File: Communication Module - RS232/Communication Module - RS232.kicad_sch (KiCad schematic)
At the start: 25 parts, among them J1 PinHeader_1x02_P2.54mm_Vertic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, P31 DB25_Receptacle_MountingHoles, U1 SP232EEN, U31 SP232EEN

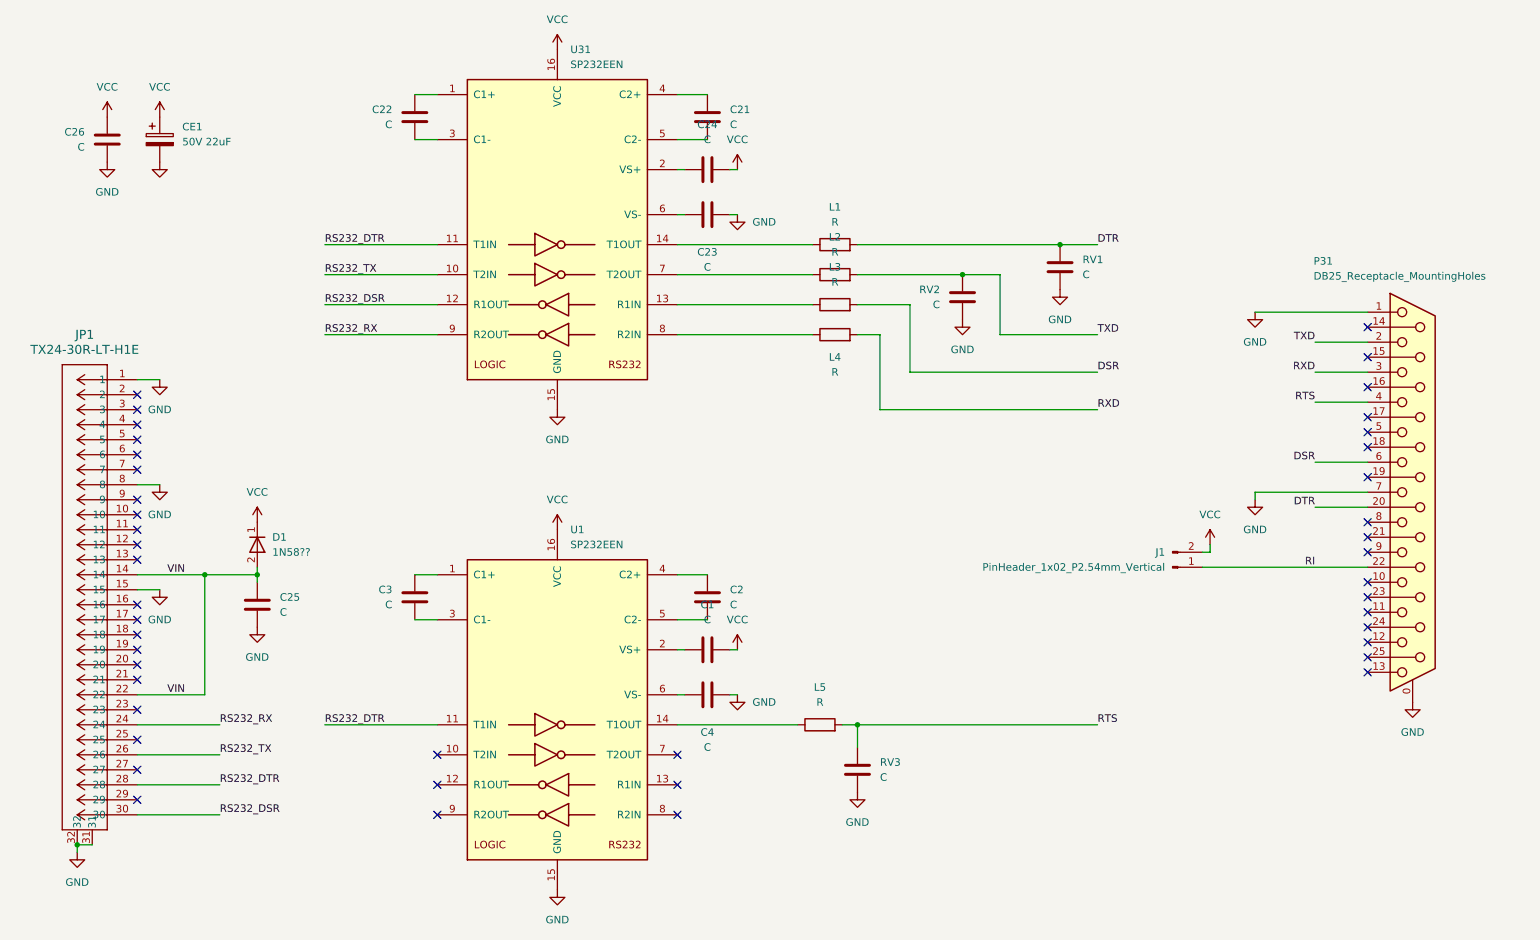
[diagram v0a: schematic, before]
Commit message: Fix net names for RS232 Communication Module
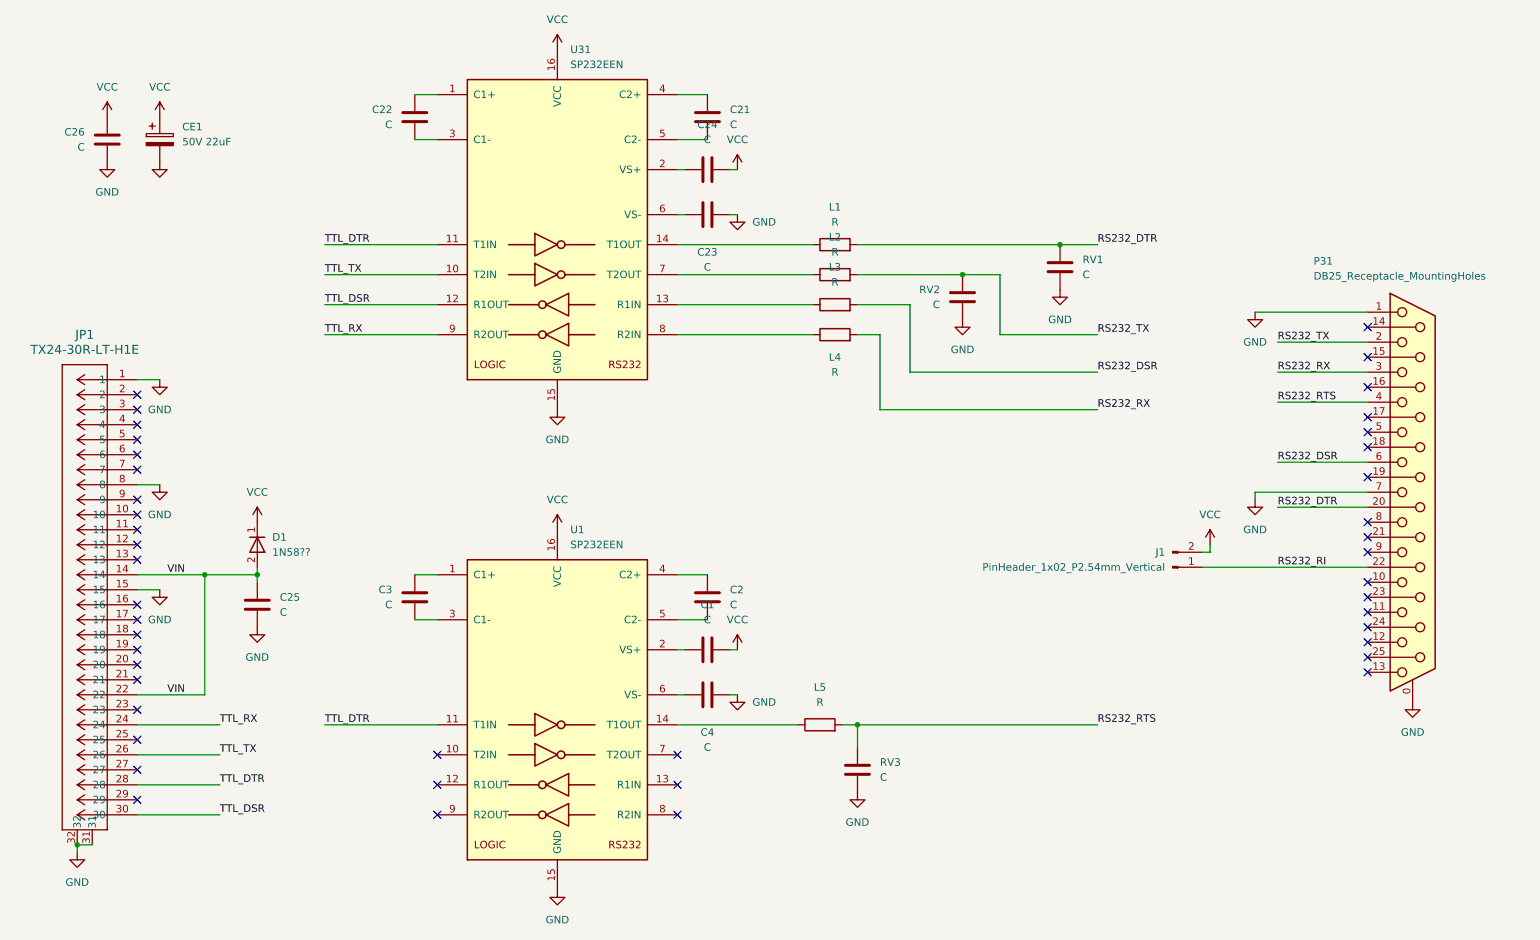
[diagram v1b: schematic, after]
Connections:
- net DSR is gone; now on net RS232_DSR: L3.2, P31.6
- net DTR is gone; now on net RS232_DTR: L1.2, P31.20 (P20), RV1.2
- net RXD is gone; now on net RS232_RX: L4.2, P31.3
- net TXD is gone; now on net RS232_TX: L2.2, P31.2, RV2.2
- net RS232_DSR: no longer JP1.30, U31.12 (R1OUT)
- net RS232_DTR: no longer JP1.28, U1.11 (T1IN), U31.11 (T1IN)
- net RS232_RX: no longer JP1.24, U31.9 (R2OUT)
- net RS232_TX: no longer JP1.26, U31.10 (T2IN)
- net RI renamed RS232_RI
- net RTS renamed RS232_RTS
- new net TTL_DSR: JP1.30, U31.12 (R1OUT)
- new net TTL_DTR: JP1.28, U1.11 (T1IN), U31.11 (T1IN)
- new net TTL_RX: JP1.24, U31.9 (R2OUT)
- new net TTL_TX: JP1.26, U31.10 (T2IN)
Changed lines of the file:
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@@
 	(wire
 		(pts
-			(xy 259.08 77.47) (xy 250.19 77.47)
+			(xy 259.08 77.47) (xy 243.84 77.47)
 		)
 		(stroke
@@
 	(wire
 		(pts
-			(xy 259.08 87.63) (xy 250.19 87.63)
+			(xy 259.08 87.63) (xy 243.84 87.63)
 		)
 		(stroke
@@
 	(wire
 		(pts
-			(xy 259.08 105.41) (xy 250.19 105.41)
+			(xy 259.08 105.41) (xy 243.84 105.41)
 		)
 		(stroke
@@
 	(wire
 		(pts
-			(xy 259.08 97.79) (xy 250.19 97.79)
+			(xy 259.08 97.79) (xy 243.84 97.79)
 		)
 		(stroke
@@
 	(wire
 		(pts
-			(xy 259.08 82.55) (xy 250.19 82.55)
+			(xy 259.08 82.55) (xy 243.84 82.55)
 		)
 		(stroke
@@
 		)
 	)
-	(label "TXD"
-		(at 250.19 77.47 180)
-		(fields_autoplaced yes)
-		(effects
-			(font
-				(size 1.27 1.27)
-			)
-			(justify right bottom)
-		)
-	)
-	(label "TXD"
+	(label "RS232_TX"
+		(at 243.84 77.47 0)
+		(fields_autoplaced yes)
+		(effects
+			(font
+				(size 1.27 1.27)
+			)
+			(justify left bottom)
+		)
+	)
+	(label "RS232_TX"
 		(at 213.36 76.2 0)
 		(fields_autoplaced yes)
@@
 		)
 	)
-	(label "DTR"
+	(label "RS232_DTR"
 		(at 213.36 60.96 0)
 		(fields_autoplaced yes)
@@
 		)
 	)
-	(label "RS232_TX"
+	(label "TTL_TX"
 		(at 64.77 147.32 0)
 		(fields_autoplaced yes)
@@
 		)
 	)
+	(label "TTL_DSR"
+		(at 82.55 71.12 0)
+		(fields_autoplaced yes)
+		(effects
+			(font
+				(size 1.27 1.27)
+			)
+			(justify left bottom)
+		)
+	)
+	(label "TTL_DTR"
+		(at 82.55 142.24 0)
+		(fields_autoplaced yes)
+		(effects
+			(font
+				(size 1.27 1.27)
+			)
+			(justify left bottom)
+		)
+	)
+	(label "TTL_RX"
+		(at 82.55 76.2 0)
+		(fields_autoplaced yes)
+		(effects
+			(font
+				(size 1.27 1.27)
+			)
+			(justify left bottom)
+		)
+	)
+	(label "RS232_RI"
+		(at 243.84 115.57 0)
+		(fields_autoplaced yes)
+		(effects
+			(font
+				(size 1.27 1.27)
+			)
+			(justify left bottom)
+		)
+	)
+	(label "TTL_RX"
+		(at 64.77 142.24 0)
+		(fields_autoplaced yes)
+		(effects
+			(font
+				(size 1.27 1.27)
+			)
+			(justify left bottom)
+		)
+	)
+	(label "RS232_RX"
+		(at 213.36 88.9 0)
+		(fields_autoplaced yes)
+		(effects
+			(font
+				(size 1.27 1.27)
+			)
+			(justify left bottom)
+		)
+	)
+	(label "RS232_RTS"
+		(at 243.84 87.63 0)
+		(fields_autoplaced yes)
+		(effects
+			(font
+				(size 1.27 1.27)
+			)
+			(justify left bottom)
+		)
+	)
+	(label "RS232_RX"
+		(at 243.84 82.55 0)
+		(fields_autoplaced yes)
+		(effects
+			(font
+				(size 1.27 1.27)
+			)
+			(justify left bottom)
+		)
+	)
 	(label "RS232_DSR"
-		(at 82.55 71.12 0)
-		(fields_autoplaced yes)
-		(effects
-			(font
-				(size 1.27 1.27)
-			)
-			(justify left bottom)
-		)
-	)
-	(label "RS232_DTR"
-		(at 82.55 142.24 0)
-		(fields_autoplaced yes)
-		(effects
-			(font
-				(size 1.27 1.27)
-			)
-			(justify left bottom)
-		)
-	)
-	(label "RS232_RX"
-		(at 82.55 76.2 0)
-		(fields_autoplaced yes)
-		(effects
-			(font
-				(size 1.27 1.27)
-			)
-			(justify left bottom)
-		)
-	)
-	(label "RI"
-		(at 250.19 115.57 180)
-		(fields_autoplaced yes)
-		(effects
-			(font
-				(size 1.27 1.27)
-			)
-			(justify right bottom)
-		)
-	)
-	(label "RS232_RX"
-		(at 64.77 142.24 0)
-		(fields_autoplaced yes)
-		(effects
-			(font
-				(size 1.27 1.27)
-			)
-			(justify left bottom)
-		)
-	)
-	(label "RXD"
-		(at 213.36 88.9 0)
-		(fields_autoplaced yes)
-		(effects
-			(font
-				(size 1.27 1.27)
-			)
-			(justify left bottom)
-		)
-	)
-	(label "RTS"
-		(at 250.19 87.63 180)
-		(fields_autoplaced yes)
-		(effects
-			(font
-				(size 1.27 1.27)
-			)
-			(justify right bottom)
-		)
-	)
-	(label "RXD"
-		(at 250.19 82.55 180)
-		(fields_autoplaced yes)
-		(effects
-			(font
-				(size 1.27 1.27)
-			)
-			(justify right bottom)
-		)
-	)
-	(label "DSR"
-		(at 250.19 97.79 180)
-		(fields_autoplaced yes)
-		(effects
-			(font
-				(size 1.27 1.27)
-			)
-			(justify right bottom)
+		(at 243.84 97.79 0)
+		(fields_autoplaced yes)
+		(effects
+			(font
+				(size 1.27 1.27)
+			)
+			(justify left bottom)
 		)
 	)
@@
 		)
 	)
-	(label "RTS"
+	(label "RS232_RTS"
 		(at 213.36 142.24 0)
 		(fields_autoplaced yes)
@@
 		)
 	)
-	(label "DSR"
+	(label "RS232_DSR"
 		(at 213.36 82.55 0)
 		(fields_autoplaced yes)
@@
 		)
 	)
+	(label "TTL_DTR"
+		(at 64.77 152.4 0)
+		(fields_autoplaced yes)
+		(effects
+			(font
+				(size 1.27 1.27)
+			)
+			(justify left bottom)
+		)
+	)
+	(label "TTL_TX"
+		(at 82.55 66.04 0)
+		(fields_autoplaced yes)
+		(effects
+			(font
+				(size 1.27 1.27)
+			)
+			(justify left bottom)
+		)
+	)
+	(label "TTL_DSR"
+		(at 64.77 157.48 0)
+		(fields_autoplaced yes)
+		(effects
+			(font
+				(size 1.27 1.27)
+			)
+			(justify left bottom)
+		)
+	)
+	(label "TTL_DTR"
+		(at 82.55 60.96 0)
+		(fields_autoplaced yes)
+		(effects
+			(font
+				(size 1.27 1.27)
+			)
+			(justify left bottom)
+		)
+	)
 	(label "RS232_DTR"
-		(at 64.77 152.4 0)
-		(fields_autoplaced yes)
-		(effects
-			(font
-				(size 1.27 1.27)
-			)
-			(justify left bottom)
-		)
-	)
-	(label "RS232_TX"
-		(at 82.55 66.04 0)
-		(fields_autoplaced yes)
-		(effects
-			(font
-				(size 1.27 1.27)
-			)
-			(justify left bottom)
-		)
-	)
-	(label "RS232_DSR"
-		(at 64.77 157.48 0)
-		(fields_autoplaced yes)
-		(effects
-			(font
-				(size 1.27 1.27)
-			)
-			(justify left bottom)
-		)
-	)
-	(label "RS232_DTR"
-		(at 82.55 60.96 0)
-		(fields_autoplaced yes)
-		(effects
-			(font
-				(size 1.27 1.27)
-			)
-			(justify left bottom)
-		)
-	)
-	(label "DTR"
-		(at 250.19 105.41 180)
-		(fields_autoplaced yes)
-		(effects
-			(font
-				(size 1.27 1.27)
-			)
-			(justify right bottom)
-		)
-	)
+		(at 243.84 105.41 0)
+		(fields_autoplaced yes)
+		(effects
+			(font
+				(size 1.27 1.27)
+			)
+			(justify left bottom)
+		)
+	)
